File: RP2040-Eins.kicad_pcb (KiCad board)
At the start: 2 copper layers, 68.6 x 53.3 mm, 55 parts, among them J1 Barrel_Jack_Switch, J10 USB_C_Receptacle_USB2.0, J2 CONN_I, J3 CONN_A, J4 CONN_P, J5 CONN_X, J7 CONN_JTAG, J8 CONN_D1, J9 CONN_D2, Q1 AO3401A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

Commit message: Moved stuff around
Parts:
- moved D3 60.1 mm to (139.7, 85.4)
- moved Y1 54.7 mm to (181.4, 95.8), turned to -90 degrees
- moved C12 54.5 mm to (141.0, 114.0), turned to 90 degrees
- moved U4 53.8 mm to (154.2, 98.3), turned to 180 degrees
- moved U6 51.9 mm to (140.8, 98.2)
- moved C17 51.1 mm to (137.9, 104.6)
- moved C16 50.8 mm to (153.4, 91.4)
- moved U2 50.5 mm to (169.1, 95.5), turned to 90 degrees
- moved D2 50.3 mm to (131.1, 104.9), turned to 180 degrees
- moved C15 48.8 mm to (152.7, 113.8), turned to 90 degrees
- moved C5 47.4 mm to (164.1, 88.9)
- moved Q1 46.9 mm to (146.6, 107.1), turned to 180 degrees
- moved C21 46.8 mm to (130.9, 97.8)
- moved R10 45.9 mm to (136.7, 85.3), turned to 90 degrees
- moved U1 45.9 mm to (154.3, 98.3), turned to 180 degrees
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
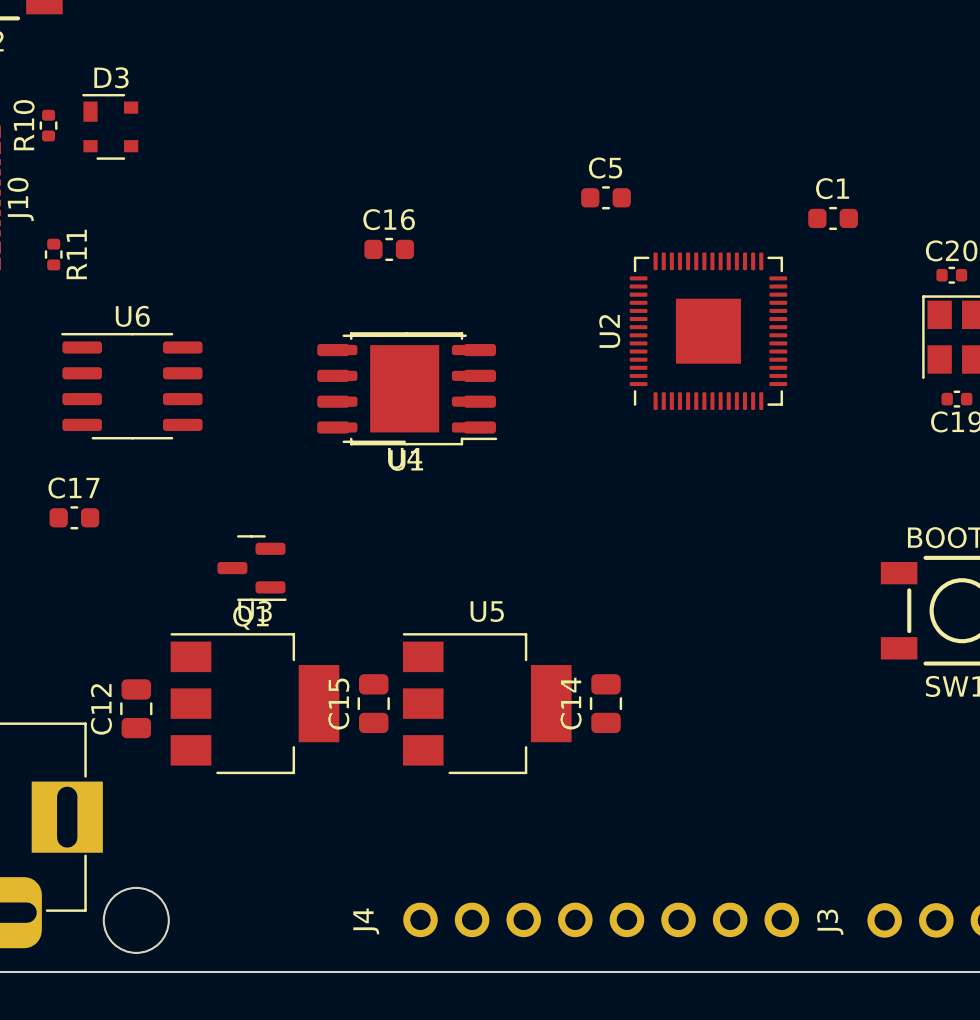
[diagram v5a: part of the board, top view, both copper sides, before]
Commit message: Added polarity reversion protection diode
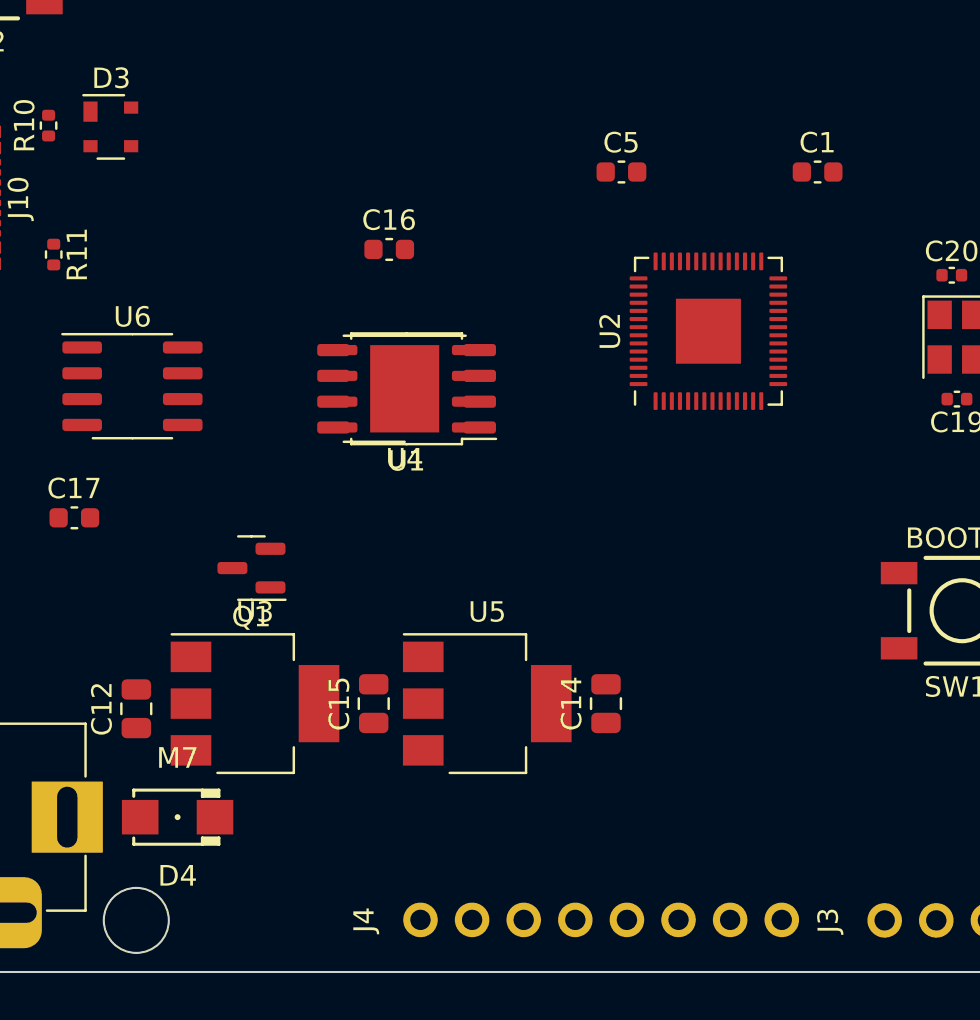
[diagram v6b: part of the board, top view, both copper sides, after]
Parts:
- added D4: M7, PCM_4ms_Diode:D_DO-214AC_SMA, F.Cu at (143.0, 119.4)
- moved C1 2.41 mm to (174.5, 87.6)
- moved C5 1.48 mm to (164.8, 87.6)
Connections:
- J1 pad 1: VIN -> Net-(D4-A)
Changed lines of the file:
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@@
   (net 64 "Net-(J10-CC2)")
   (net 65 "unconnected-(J10-SBU2-PadB8)")
+  (net 66 "Net-(D4-A)")
   (footprint "Package_TO_SOT_SMD:SOT-23" (layer "F.Cu")
     (at 146.6365 107.122 180)
@@
   )
   (footprint "Capacitor_SMD:C_0603_1608Metric" (layer "F.Cu")
-    (at 164.084 88.9)
+    (at 164.846 87.63)
     (descr "Capacitor SMD 0603 (1608 Metric), square (rectangular) end terminal, IPC_7351 nominal, (Body size source: IPC-SM-782 page 76, https://www.pcb-3d.com/wordpress/wp-content/uploads/ipc-sm-782a_amendment_1_and_2.pdf), generated with kicad-footprint-generator")
     (tags "capacitor")
@@
       (stroke (width 0.1) (type solid)) (layer "F.Fab"))
     (pad "1" thru_hole rect (at 0 0) (size 3.5 3.5) (drill oval 1 3) (layers "*.Cu" "*.Mask")
-      (net 5 "VIN") (pintype "passive"))
+      (net 66 "Net-(D4-A)") (pintype "passive"))
     (pad "2" thru_hole roundrect (at -6 0) (size 3 3.5) (drill oval 1 3) (layers "*.Cu" "*.Mask") (roundrect_rratio 0.25)
       (net 4 "GND") (pintype "passive"))
@@
   )
   (footprint "Capacitor_SMD:C_0603_1608Metric" (layer "F.Cu")
-    (at 175.26 89.916)
+    (at 174.498 87.63)
     (descr "Capacitor SMD 0603 (1608 Metric), square (rectangular) end terminal, IPC_7351 nominal, (Body size source: IPC-SM-782 page 76, https://www.pcb-3d.com/wordpress/wp-content/uploads/ipc-sm-782a_amendment_1_and_2.pdf), generated with kicad-footprint-generator")
     (tags "capacitor")
@@
       (offset (xyz 0 0 0))
       (scale (xyz 1 1 1))
+      (rotate (xyz 0 0 0))
+    )
+  )
+  (footprint "PCM_4ms_Diode:D_DO-214AC_SMA" (layer "F.Cu")
+    (at 143.002 119.38 180)
+    (descr "Diode DO-214AC (SMA) Vishay")
+    (tags "Diode SMA")
+    (property "Sheetfile" "RP2040-Eins.kicad_sch")
+    (property "Sheetname" "")
+    (property "ki_description" "SMA Diode, Rectifier, 1000V, 1A, Alternate KiCad Library")
+    (property "ki_keywords" "diode M7 4007")
+    (attr smd)
+    (fp_text reference "D4" (at 0 -2.9) (layer "F.SilkS")
+        (effects (font (size 1.016 1.016) (thickness 0.1524)))
+    )
+    (fp_text value "M7" (at 0 2.9) (layer "F.SilkS")
+        (effects (font (size 1.016 1.016) (thickness 0.1524)))
+    )
+    (fp_line (start -2.032 -1.3325) (end -2.032 -1.0245)
+      (stroke (width 0.15) (type solid)) (layer "F.SilkS"))
+    (fp_line (start -2.032 -1.3325) (end 2.159 -1.3325)
+      (stroke (width 0.15) (type solid)) (layer "F.SilkS"))
+    (fp_line (start -2.032 1.3325) (end -2.032 1.0245)
+      (stroke (width 0.15) (type solid)) (layer "F.SilkS"))
+    (fp_line (start -2.032 1.3325) (end 2.159 1.3325)
+      (stroke (width 0.15) (type solid)) (layer "F.SilkS"))
+    (fp_line (start -1.9156 -1.18) (end -1.33 -1.18)
+      (stroke (width 0.3) (type solid)) (layer "F.SilkS"))
+    (fp_line (start -1.89 1.17) (end -1.34 1.17)
+      (stroke (width 0.3) (type solid)) (layer "F.SilkS"))
+    (fp_line (start -1.2192 -1.3325) (end -1.2192 -1.0245)
+      (stroke (width 0.15) (type solid)) (layer "F.SilkS"))
+    (fp_line (start -1.2192 -1.0245) (end -2.032 -1.0245)
+      (stroke (width 0.15) (type solid)) (layer "F.SilkS"))
+    (fp_line (start -1.2192 1.0245) (end -2.032 1.0245)
+      (stroke (width 0.15) (type solid)) (layer "F.SilkS"))
+    (fp_line (start -1.2192 1.3325) (end -1.2192 1.0245)
+      (stroke (width 0.15) (type solid)) (layer "F.SilkS"))
+    (fp_line (start 2.159 -1.3325) (end 2.159 -1.0245)
+      (stroke (width 0.15) (type solid)) (layer "F.SilkS"))
+    (fp_line (start 2.159 1.3325) (end 2.159 1.0245)
+      (stroke (width 0.15) (type solid)) (layer "F.SilkS"))
+    (fp_circle (center 0 0) (end 0.0762 -0.0254)
+      (stroke (width 0.127) (type solid)) (fill none) (layer "F.SilkS"))
+    (fp_line (start -3 -1.6575) (end 3 -1.6575)
+      (stroke (width 0.05) (type solid)) (layer "F.CrtYd"))
+    (fp_line (start -3 1.6575) (end -3 -1.6575)
+      (stroke (width 0.05) (type solid)) (layer "F.CrtYd"))
+    (fp_line (start 3 -1.6575) (end 3 1.6575)
+      (stroke (width 0.05) (type solid)) (layer "F.CrtYd"))
+    (fp_line (start 3 1.6575) (end -3 1.6575)
+      (stroke (width 0.05) (type solid)) (layer "F.CrtYd"))
+    (pad "1" smd rect (at -1.84 0 180) (size 1.8 1.7) (layers "F.Cu" "F.Paste" "F.Mask")
+      (net 5 "VIN") (pinfunction "K") (pintype "passive"))
+    (pad "2" smd rect (at 1.84 0 180) (size 1.8 1.7) (layers "F.Cu" "F.Paste" "F.Mask")
+      (net 66 "Net-(D4-A)") (pinfunction "A") (pintype "passive"))
+    (model "${KISYS3DMOD}/Diode_SMD.3dshapes/D_SMA.wrl"
+      (offset (xyz 0 0 0))
+      (scale (xyz 1 1 1))

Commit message: Moved stuff around
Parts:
- added C22: 100nF, Capacitor_SMD:C_0402_1005Metric, F.Cu at (162.3, 96.0)
- moved R6 64.9 mm to (133.9, 104.9)
- moved R9 60.1 mm to (146.1, 99.6), turned to 90 degrees
- moved R1 58.9 mm to (133.9, 108.7), turned to 180 degrees
- moved R8 57.6 mm to (146.1, 101.9), turned to 90 degrees
- moved C13 51.3 mm to (180.6, 90.9)
- moved C7 49.5 mm to (175.8, 94.0)
- moved C4 48.8 mm to (166.4, 88.2), turned to 90 degrees
- moved C3 47.8 mm to (170.2, 88.1), turned to 90 degrees
- moved C6 46.8 mm to (175.8, 95.0)
- moved R5 45.5 mm to (180.6, 89.9), turned to 180 degrees
- moved C8 42.2 mm to (170.4, 101.9), turned to -90 degrees
- moved C18 41.7 mm to (138.2, 105.2), turned to 180 degrees
- moved C9 40.4 mm to (162.3, 91.9), turned to 180 degrees
- moved C10 39.3 mm to (162.3, 95.0), turned to 180 degrees
- moved C11 34.9 mm to (166.6, 101.9), turned to -90 degrees
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
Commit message: Moved stuff around
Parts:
- moved R1 5.86 mm to (133.3, 102.9)
- moved D1 5.85 mm to (130.8, 102.9)
- moved R6 3.09 mm to (133.3, 108.0)
- moved D2 3.06 mm to (130.8, 108.0)
- moved U1 2.12 mm to (153.7, 100.3)
- moved U4 2.09 mm to (153.7, 100.3)
- moved C16 1.93 mm to (153.4, 104.1)
- moved C2 1.85 mm to (150.9, 104.1)
- moved C5 1.83 mm to (161.3, 89.2)
- moved C9 1.83 mm to (161.3, 90.4)
- moved Q1 1.78 mm to (146.1, 107.4)
- moved C18 1.19 mm to (138.5, 104.0)
- moved C17 1.19 mm to (141.0, 104.0)
- moved U6 1.19 mm to (141.0, 100.3)
- moved C8 1.02 mm to (170.2, 102.9)
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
